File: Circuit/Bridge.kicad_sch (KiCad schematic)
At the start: 40 parts, among them K2 AGQ200A12, Q4 TIP41C, Q5 TIP42C, Q6 TIP41C, Q7 TIP42C, U10 OPA2197xD, U6 OPA2197xD, U7 ULN2003, U8 DG201, U9 OPA2376xxD

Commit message: Output job, Revision Box and reorganise
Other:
- company: Harry and Yuki - EEE3 Instrumentation -> Harry Hill and Yuki Hoshino
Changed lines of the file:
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@@
 	(title_block
 		(title "Auto-Balancing Bridge")
-		(date "2026-03-02")
+		(date "2026-05-02")
 		(rev "1.0")
-		(company "Harry and Yuki - EEE3 Instrumentation")
+		(company "Harry Hill and Yuki Hoshino")
+		(comment 1 "LCR Meter")
 	)
 	(rectangle

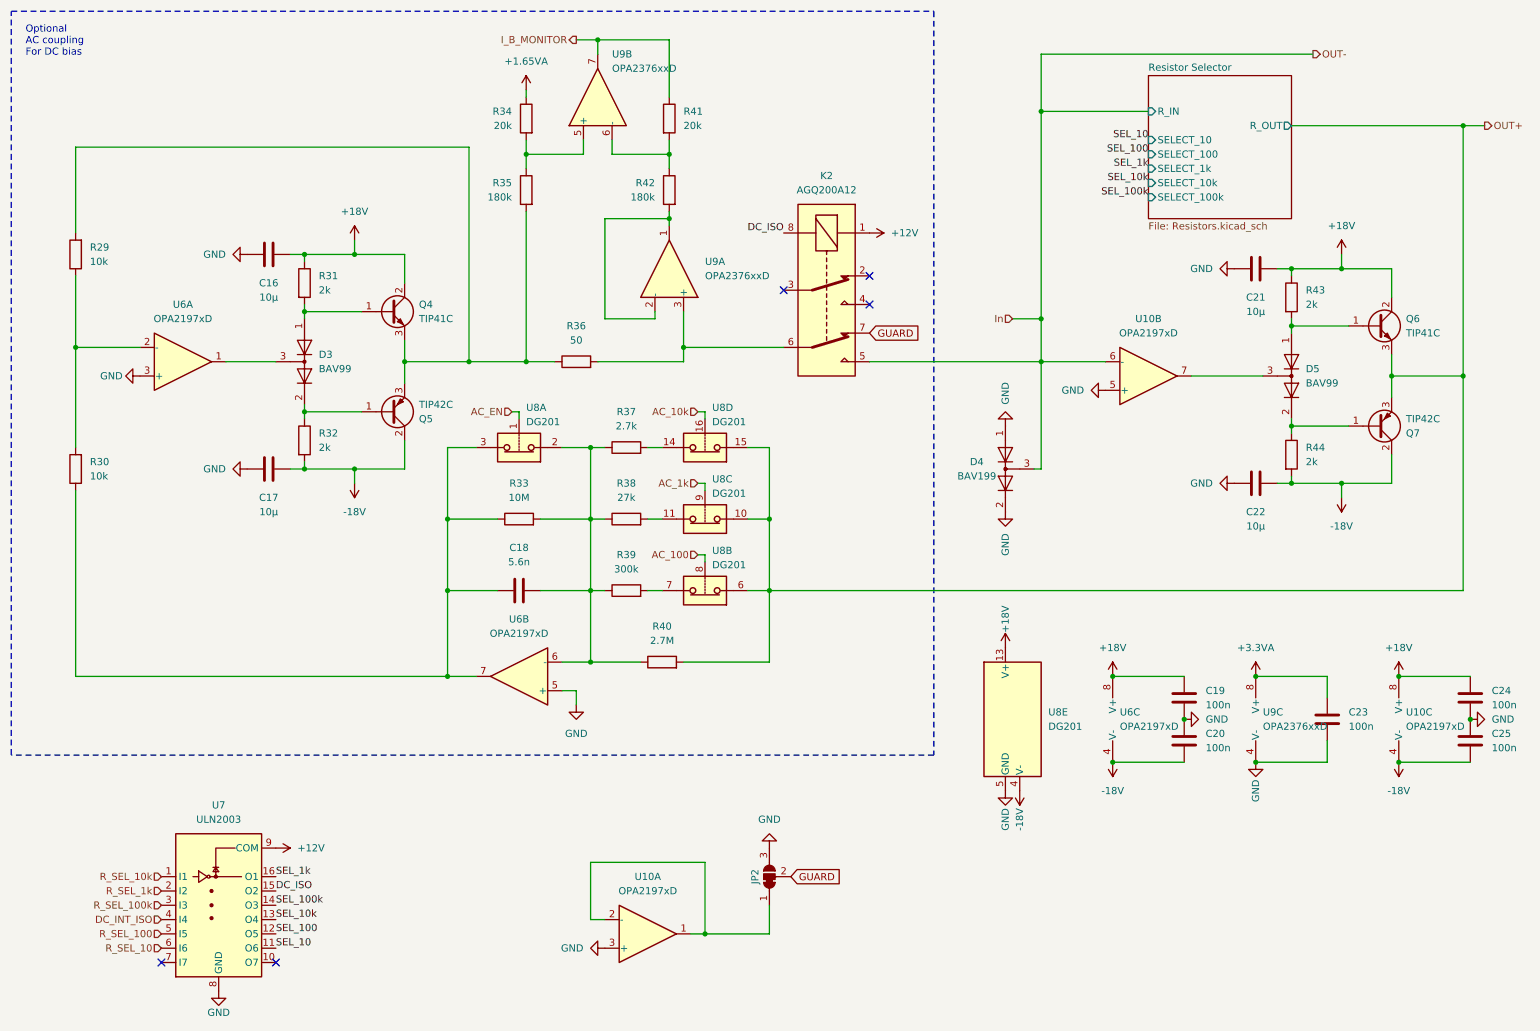
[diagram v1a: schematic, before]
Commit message: Input Protection Second Attempt
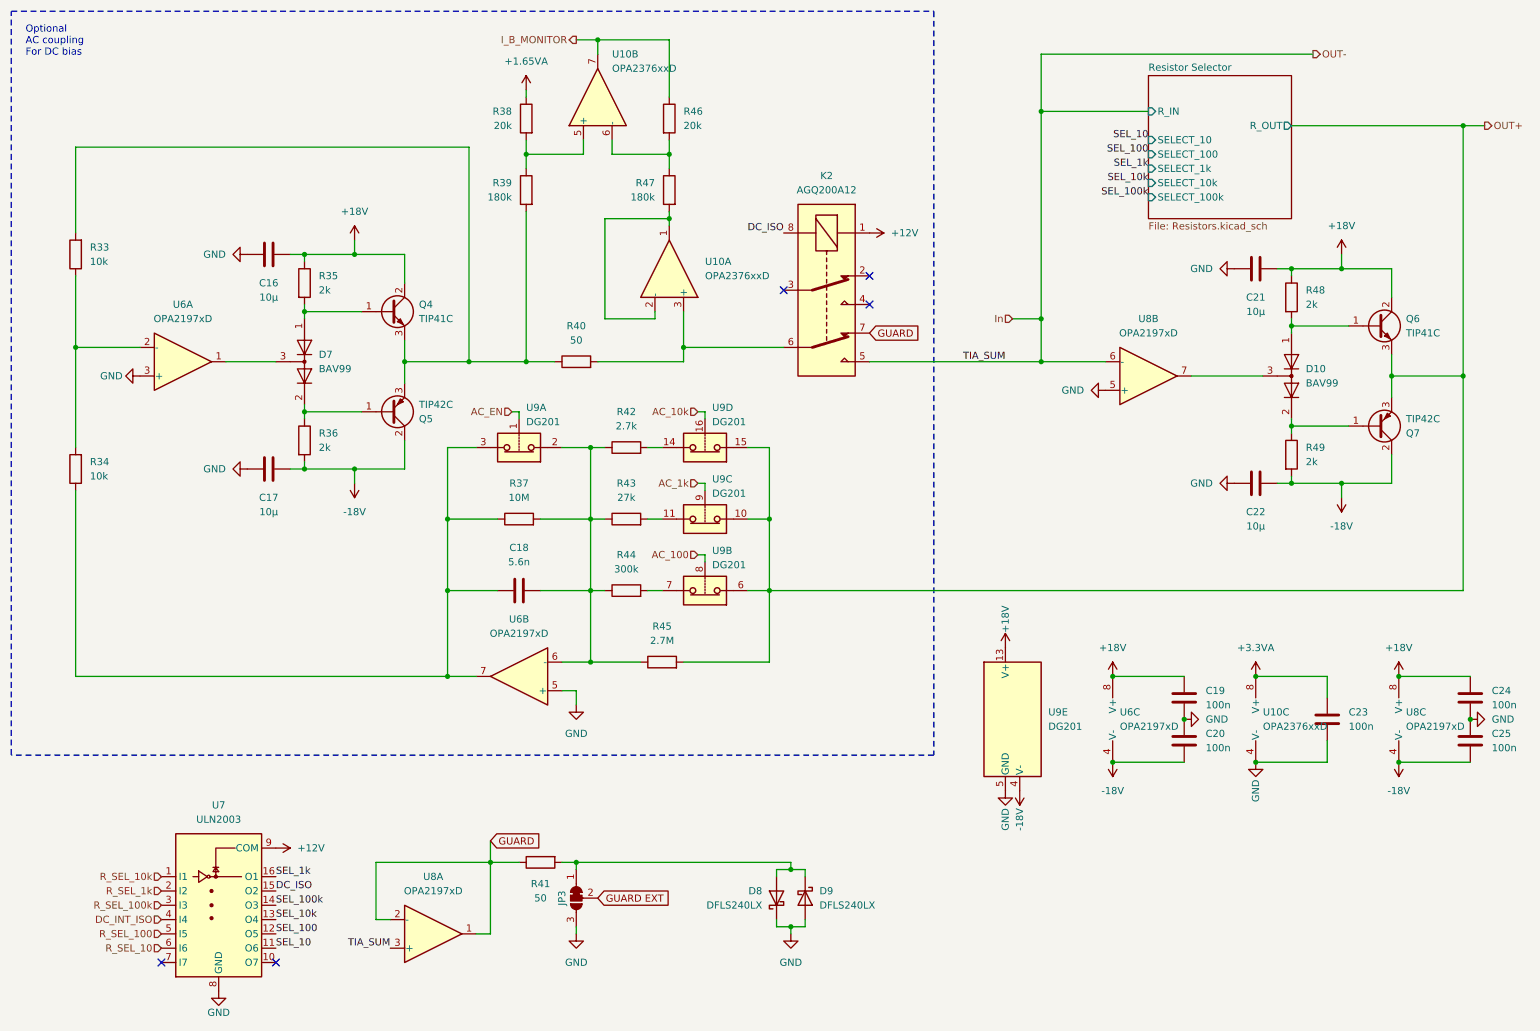
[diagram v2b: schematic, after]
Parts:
- removed D4: BAV199, Package_TO_SOT_SMD:SOT-23, symbol Diode:BAV99
- removed JP2: SolderJumper_3_Bridged12, Jumper:SolderJumper-3_P1.3mm_Bridged12_RoundedPad1.0x1.5mm, symbol Jumper:SolderJumper_3_Bridged12
- added D8, D9: DFLS240LX, Diode_SMD:D_PowerDI-123, symbol Device:D_Schottky
- added JP3: SolderJumper_3_Bridged12, Jumper:SolderJumper-3_P1.3mm_Bridged12_RoundedPad1.0x1.5mm, symbol Jumper:SolderJumper_3_Bridged12
- added R41: 50, Resistor_SMD:R_0805_2012Metric, symbol Device:R
- renumbered D5 to D10, D3 to D7, R29 to R33, R30 to R34, R31 to R35, R32 to R36, R33 to R37, R34 to R38, R35 to R39, R36 to R40, R37 to R42, R38 to R43, R39 to R44, R40 to R45, R41 to R46, R42 to R47, R43 to R48, R44 to R49, U9 to U10, U10 to U8, U8 to U9
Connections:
- net GND: now also D8.1 (K), D9.2 (A), JP3.3 (B); no longer U8.3 (+)
- net GUARD: now also U8.1, U8.2 (-), R41.1
- net In: now also U8.3 (+)
- new net: D8.2 (A), D9.1 (K), JP3.1 (A), R41.2
- new net GUARD EXT: JP3.2 (C)
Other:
- moved on the sheet: U8A

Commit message: New Resistor Selection Circuit
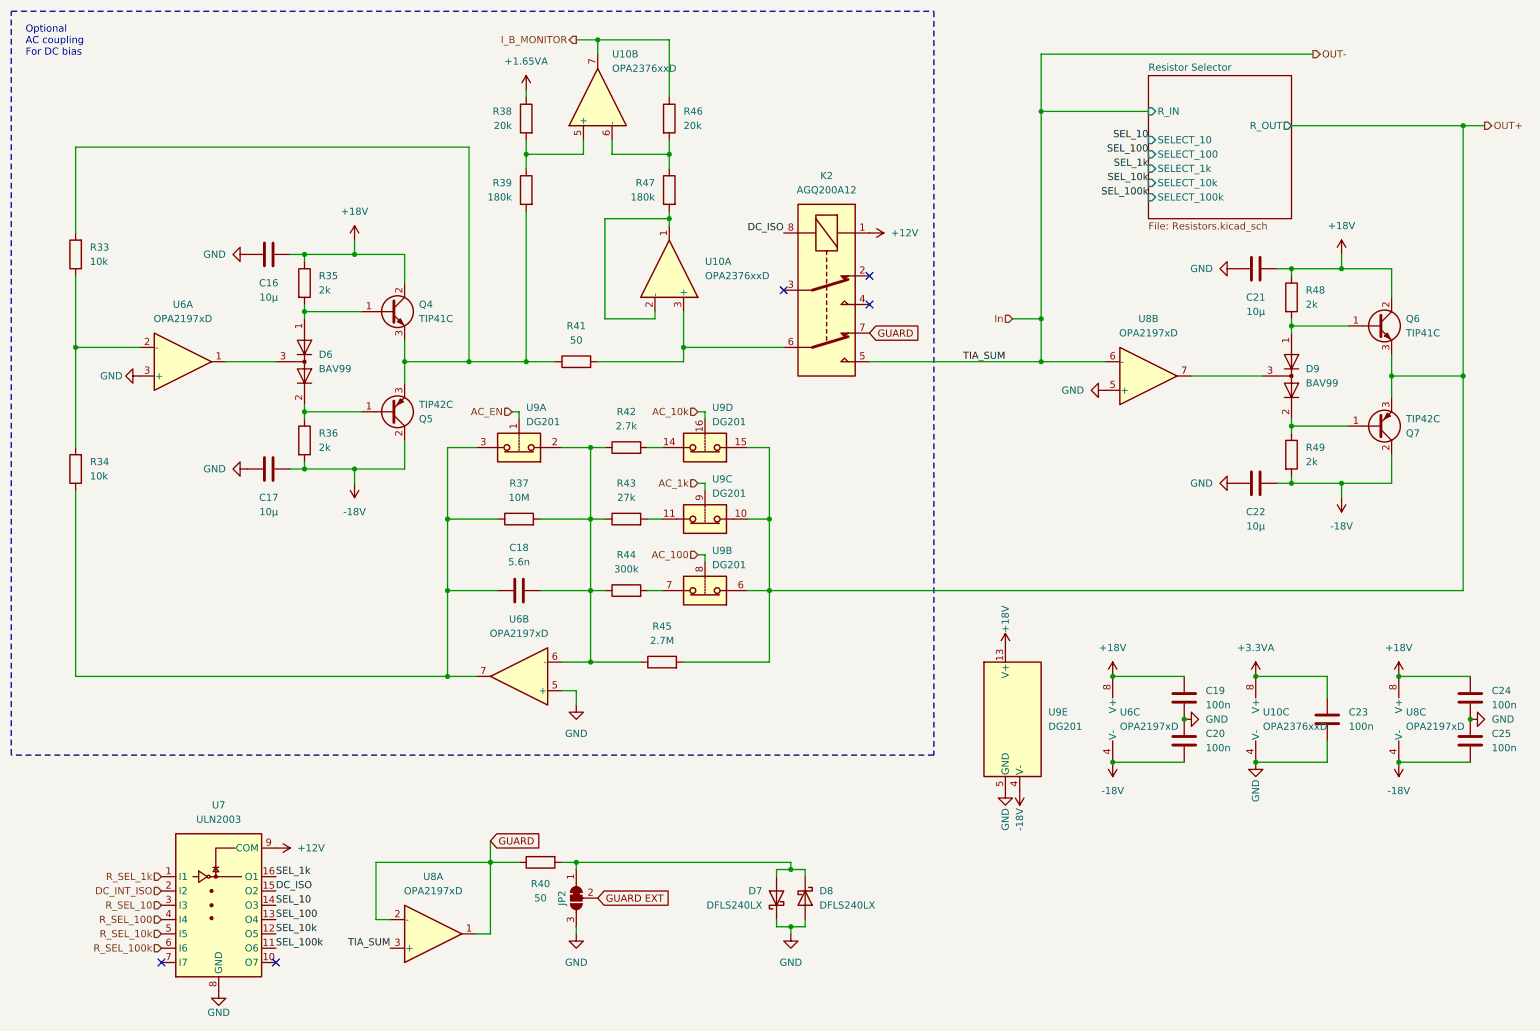
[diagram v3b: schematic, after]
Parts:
- renumbered D7 to D6, D8 to D7, D9 to D8, D10 to D9, JP3 to JP2, R41 to R40, R40 to R41
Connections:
- net DC_INT_ISO: now also U7.2 (I2); no longer U7.4 (I4)
- net R_SEL_10: now also U7.3 (I3); no longer U7.6 (I6)
- net R_SEL_100: now also U7.4 (I4); no longer U7.5 (I5)
- net R_SEL_100k: now also U7.6 (I6); no longer U7.3 (I3)
- net R_SEL_10k: now also U7.5 (I5); no longer U7.1 (I1)
- net R_SEL_1k: now also U7.1 (I1); no longer U7.2 (I2)
- net SEL_10: now also U7.14 (O3); no longer U7.11 (O6)
- net SEL_100: now also U7.13 (O4); no longer U7.12 (O5)
- net SEL_100k: now also U7.11 (O6); no longer U7.14 (O3)
- net SEL_10k: now also U7.12 (O5); no longer U7.13 (O4)
